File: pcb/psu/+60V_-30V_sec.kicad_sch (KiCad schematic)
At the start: 51 parts, among them J3 Conn_01x03_Socket, J4 Conn_01x03_Socket, U5 ADPL54203, U6 ADPL54203

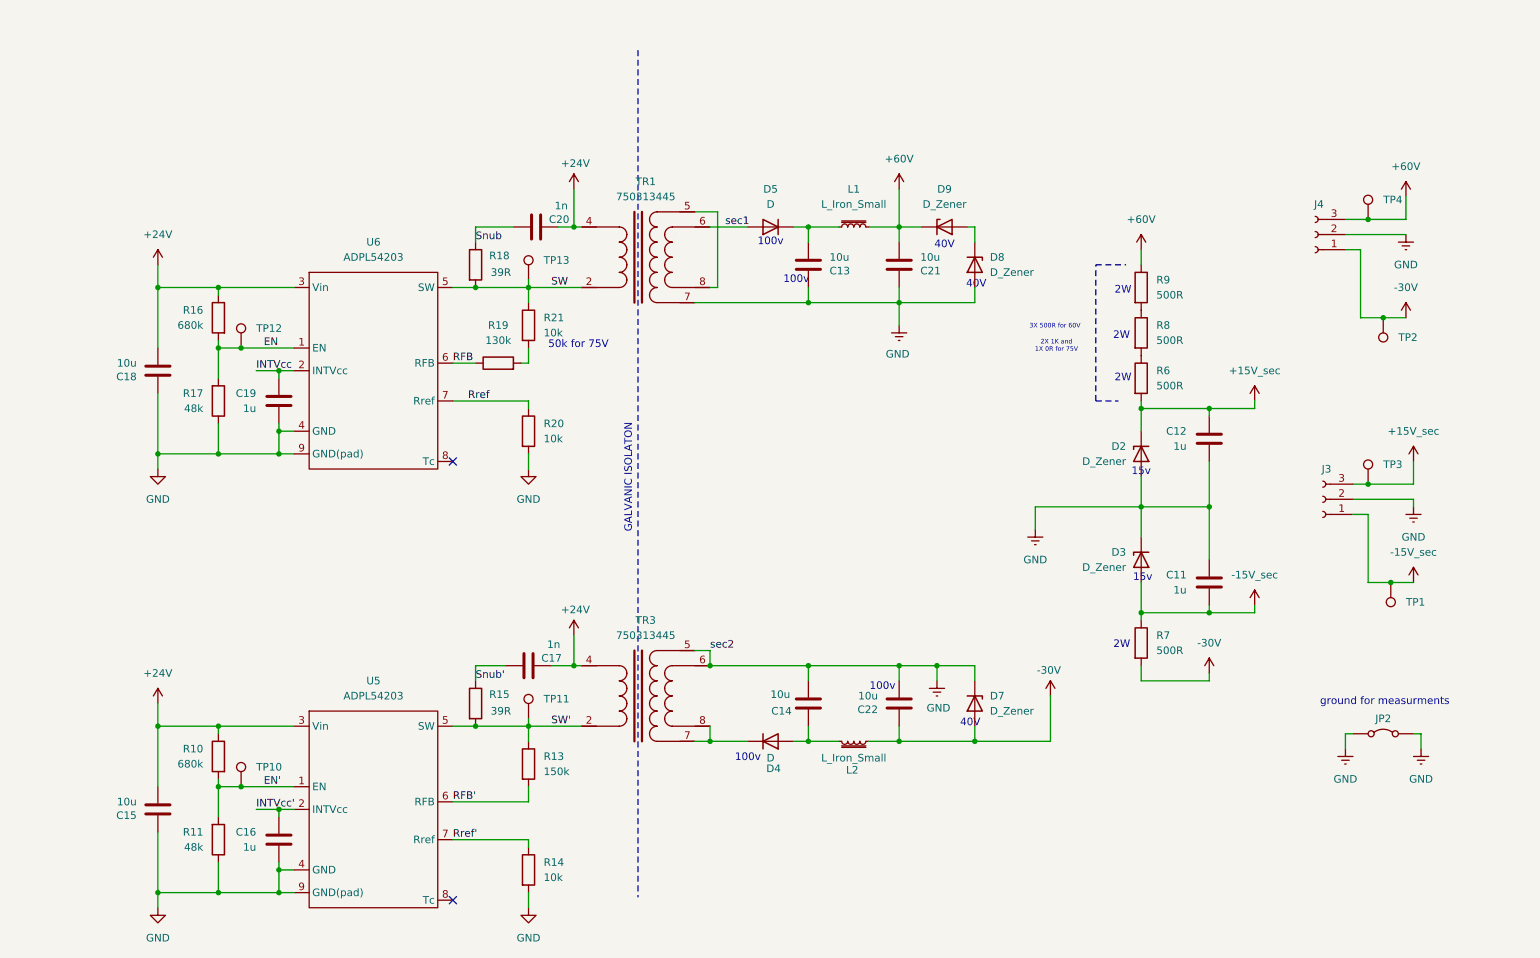
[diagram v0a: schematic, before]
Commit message: poprawki do schematu psu
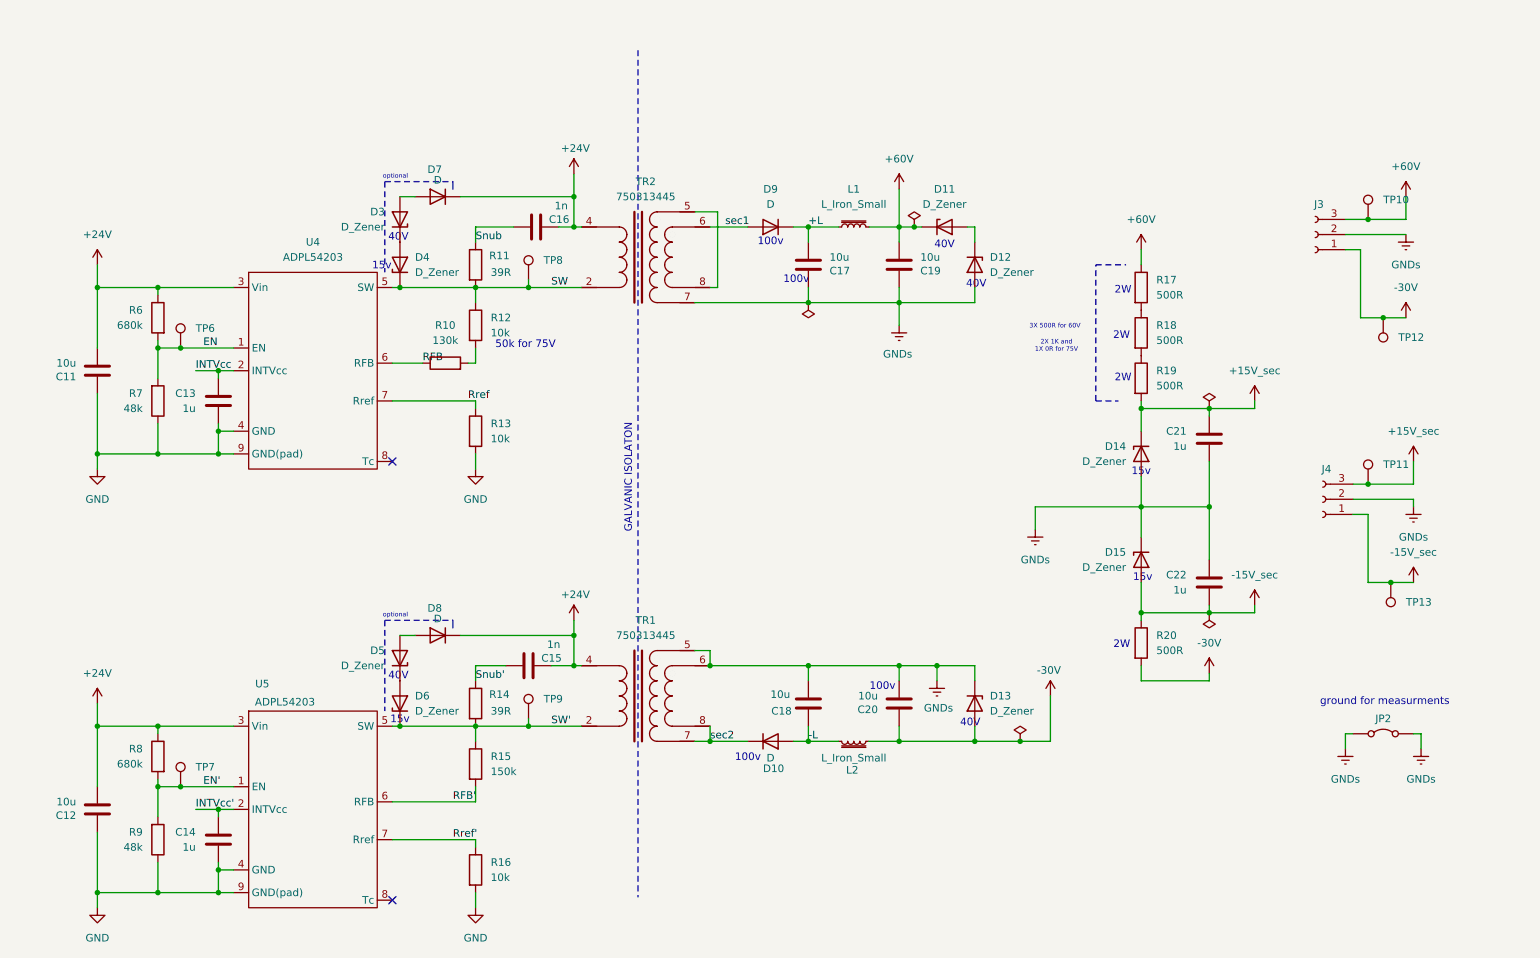
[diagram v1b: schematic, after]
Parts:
- removed TR3: 750313445, Transformer_SMD:Transformer_Wurth_WE-AGDT-EP7, symbol New_Library:750313445
- added D3, D4, D5, D6: D_Zener, symbol Device:D_Zener
- added D7, D8: D, symbol Device:D
- added TR2: 750313445, Library:750313445, symbol New_Library:750313445
- TR1: footprint Transformer_SMD:Transformer_Wurth_WE-AGDT-EP7 -> Library:750313445
- renumbered C18 to C11, C15 to C12, C19 to C13, C16 to C14, C17 to C15, C20 to C16, C13 to C17, C14 to C18, C21 to C19, C22 to C20, C12 to C21, C11 to C22, D4 to D10, D9 to D11, D8 to D12, D7 to D13, D2 to D14, D3 to D15, D5 to D9, J4 to J3, J3 to J4, R19 to R10, R18 to R11, R21 to R12, R20 to R13, R15 to R14, R13 to R15, R14 to R16, R9 to R17, R8 to R18, R6 to R19, R7 to R20, R16 to R6, R17 to R7, R10 to R8, R11 to R9, TP4 to TP10, TP3 to TP11, TP2 to TP12, TP1 to TP13, TP12 to TP6, TP10 to TP7, TP13 to TP8, TP11 to TP9, U6 to U4
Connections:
- net +24V: now also D7.1 (K), D8.1 (K), TR2.4
- net GND: no longer C17.1, C18.2, C19.1, C20.2, C21.2, C22.1, D12.2 (A), D13.1 (K), D14.2 (A), D15.1 (K), J3.2 (Pin_2), J4.2 (Pin_2), JP2.1 (A), JP2.2 (B), TR1.7
- net SW: now also D4.1 (K), TR2.2; no longer TR1.2
- net SW': now also TR1.2, D6.1 (K)
- net sec1: now also TR2.6; no longer TR1.6
- net -L: now reaches C18.1, D10.2 (A), L2.2
- net GNDs: now reaches TR1.5
- net GNDs: now also C17.1, C18.2, C19.1, C20.2, C21.2, C22.1, D12.2 (A), D13.1 (K), D14.2 (A), D15.1 (K), J3.2 (Pin_2), J4.2 (Pin_2), JP2.1 (A), JP2.2 (B), TR1.6, TR2.7; no longer TR1.8
- net +L: now reaches C17.2, D9.1 (K), L1.1
- net sec2: now reaches D10.1 (K)
- net sec2: now also TR1.7, TR1.8
- new net: D5.1 (K), D6.2 (A)
- new net: D5.2 (A), D8.2 (A)
- new net: D3.1 (K), D4.2 (A)
- new net: TR2.5, TR2.8
- new net: D3.2 (A), D7.2 (A)
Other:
- note added: "optional"
- moved on the sheet: C11, C12, C13, C14, R10, R12, R13, R15, R16, R6, R7, R8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

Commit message: added PSU PCB design files
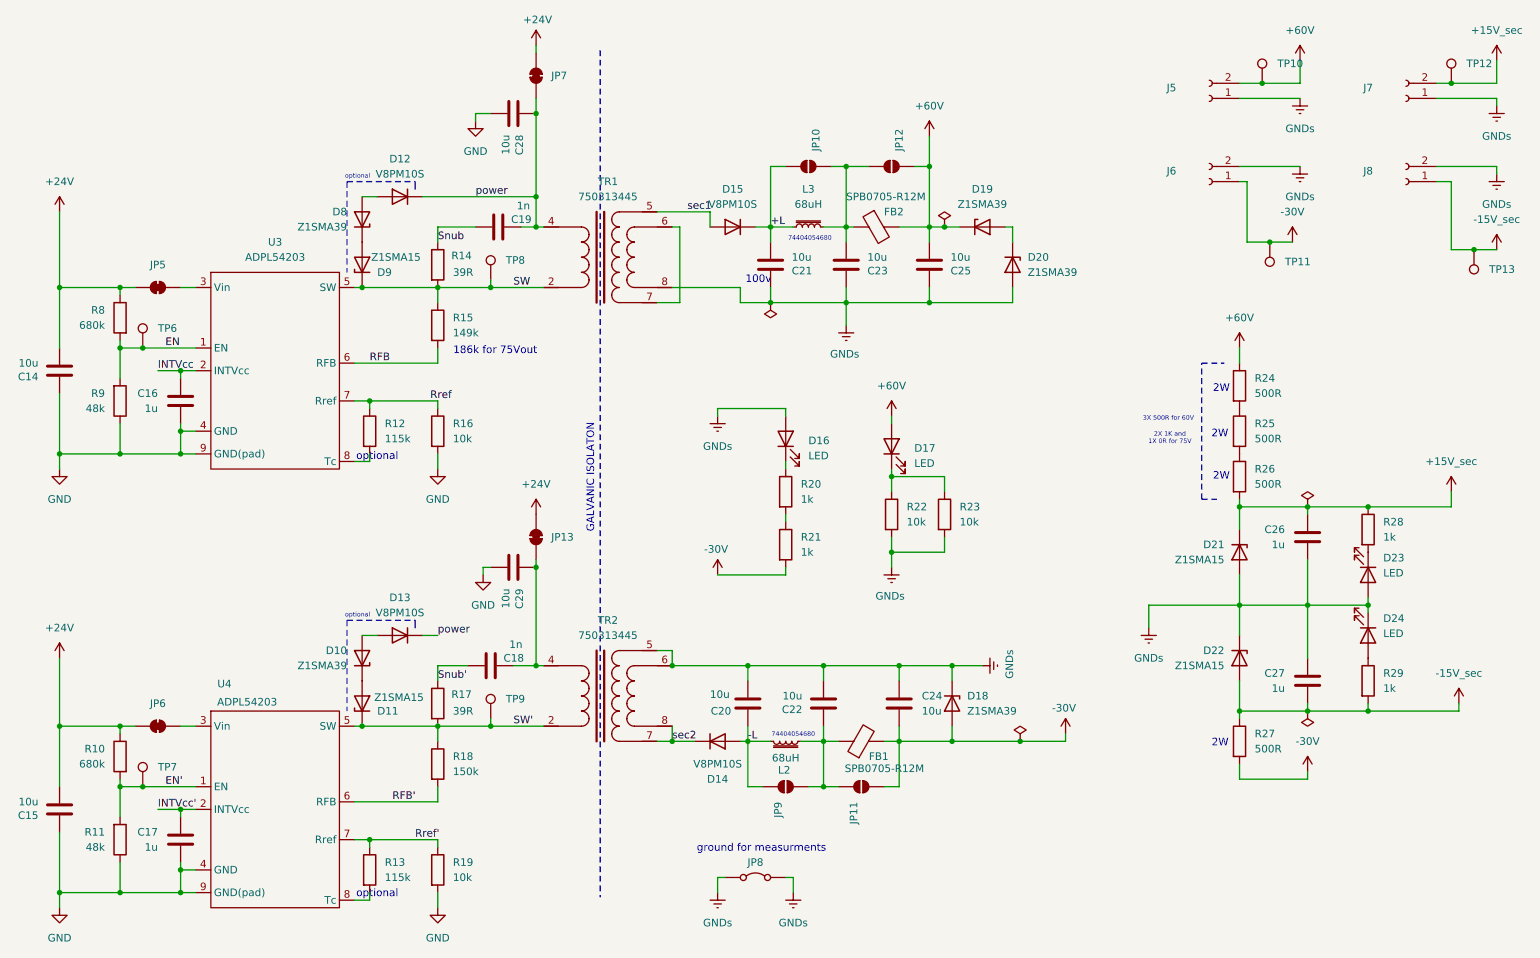
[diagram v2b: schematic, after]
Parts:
- removed D10, D7, D8, D9: D, symbol Device:D
- removed D11, D12, D13, D14, D15, D3, D4, D5, D6: D_Zener, symbol Device:D_Zener
- removed J3, J4: Conn_01x03_Socket, symbol Connector:Conn_01x03_Socket
- removed R10: 130k, symbol Device:R
- added C24, C28, C29: 10u, Capacitor_SMD:C_0805_2012Metric, symbol Device:C
- added C25: 10u, Capacitor_SMD:C_1210_3225Metric, symbol Device:C
- added D10, D18, D19, D20, D8: Z1SMA39, Diode_SMD:D_SMA, symbol Diode:Z1SMAxxx
- added D11, D21, D22, D9: Z1SMA15, Diode_SMD:D_SMA, symbol Diode:Z1SMAxxx
- added D12, D13, D14, D15: V8PM10S, Package_TO_SOT_SMD:TO-277A, symbol Diode:VS-6ESU06
- added D16, D17, D23, D24: LED, LED_SMD:LED_0603_1608Metric, symbol Device:LED
- added FB1, FB2: SPB0705-R12M, Inductor_SMD:L_Coilcraft_1515SQ-68N, symbol Device:FerriteBead
- added J5, J6, J7, J8: Conn_01x02_Socket, Connector_Wago:Wago_734-132_1x02_P3.50mm_Vertical, symbol Connector:Conn_01x02_Socket
- added JP10, JP11, JP12, JP9: SolderJumper_2_Open, Jumper:SolderJumper-2_P1.3mm_Open_RoundedPad1.0x1.5mm, symbol Jumper:SolderJumper_2_Open
- added JP13, JP5, JP6, JP7: SolderJumper_2_Bridged, Jumper:SolderJumper-2_P1.3mm_Bridged2Bar_RoundedPad1.0x1.5mm, symbol Jumper:SolderJumper_2_Bridged
- added R12, R13: 115k, Resistor_SMD:R_0805_2012Metric, symbol Device:R
- added R20, R21, R28, R29: 1k, Resistor_SMD:R_0805_2012Metric, symbol Device:R
- added R22, R23: 10k, Resistor_SMD:R_0805_2012Metric, symbol Device:R
- C14: renamed from C11; footprint (none) -> Capacitor_SMD:C_0805_2012Metric
- C15: renamed from C12; footprint (none) -> Capacitor_SMD:C_0805_2012Metric
- C16: renamed from C13; footprint (none) -> Capacitor_SMD:C_0805_2012Metric
- C17: renamed from C14; footprint (none) -> Capacitor_SMD:C_0805_2012Metric
- C18: renamed from C15; footprint (none) -> Capacitor_SMD:C_0805_2012Metric
- C19: renamed from C16; footprint (none) -> Capacitor_SMD:C_0805_2012Metric
- C20: renamed from C18; footprint (none) -> Capacitor_SMD:C_0805_2012Metric
- C21: renamed from C17; footprint (none) -> Capacitor_SMD:C_1210_3225Metric
- C22: renamed from C20; footprint (none) -> Capacitor_SMD:C_0805_2012Metric
- C23: renamed from C19; footprint (none) -> Capacitor_SMD:C_1210_3225Metric
- C26: renamed from C21; footprint (none) -> Capacitor_SMD:C_0805_2012Metric
- C27: renamed from C22; footprint (none) -> Capacitor_SMD:C_0805_2012Metric
- JP8: renamed from JP2; footprint (none) -> Capacitor_THT:C_Axial_L12.0mm_D6.5mm_P15.00mm_Horizontal
- L2: value L_Iron_Small -> 68uH; footprint (none) -> Inductor_SMD:L_Wuerth_MAPI-5030
- L3: renamed from L1; value L_Iron_Small -> 68uH; footprint (none) -> Inductor_SMD:L_Wuerth_MAPI-5030
- R10: renamed from R8; footprint (none) -> Resistor_SMD:R_0805_2012Metric
- R11: renamed from R9; footprint (none) -> Resistor_SMD:R_0805_2012Metric
- R14: renamed from R11; footprint (none) -> Resistor_SMD:R_2512_6332Metric
- R15: renamed from R12; value 10k -> 149k; footprint (none) -> Resistor_SMD:R_0805_2012Metric
- R16: renamed from R13; footprint (none) -> Resistor_SMD:R_0805_2012Metric
- R17: renamed from R14; footprint (none) -> Resistor_SMD:R_2512_6332Metric
- R18: renamed from R15; footprint (none) -> Resistor_SMD:R_0805_2012Metric
- R19: renamed from R16; footprint (none) -> Resistor_SMD:R_0805_2012Metric
- R24: renamed from R17; footprint (none) -> Resistor_SMD:R_2512_6332Metric
- R25: renamed from R18; footprint (none) -> Resistor_SMD:R_2512_6332Metric
- R26: renamed from R19; footprint (none) -> Resistor_SMD:R_2512_6332Metric
- R27: renamed from R20; footprint (none) -> Resistor_SMD:R_2512_6332Metric
- R8: renamed from R6; footprint (none) -> Resistor_SMD:R_0805_2012Metric
- R9: renamed from R7; footprint (none) -> Resistor_SMD:R_0805_2012Metric
- TP10, TP13, TP6, TP7, TP8, TP9: footprint (none) -> TestPoint:TestPoint_Pad_D1.5mm
- TP11: renamed from TP12; footprint (none) -> TestPoint:TestPoint_Pad_D1.5mm
- TP12: renamed from TP11; footprint (none) -> TestPoint:TestPoint_Pad_D1.5mm
- renumbered TR2 to TR1, TR1 to TR2, U4 to U3, U5 to U4
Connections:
- net +15V_sec: now also D21.1 (K), J7.2 (Pin_2), R28.1
- net +24V: now also JP13.1 (A), JP5.2 (B), JP6.2 (B), JP7.2 (B); no longer C18.2, C19.2, TR1.4, TR2.4, U3.3 (Vin), U4.3 (Vin)
- net +60V: now also C25.2, D17.2 (A), D19.1 (K), FB2.2, J5.2 (Pin_2), JP12.1 (A); no longer C23.2, L3.2
- net +L: now also D15.3 (K), JP10.2 (B)
- net -15V_sec: now also D22.2 (A), J8.1 (Pin_1), R29.2
- net -30V: now also C24.2, D18.2 (A), FB1.2, J6.1 (Pin_1), JP11.2 (B), R21.2; no longer C22.1, L2.1
- net -L: now also D14.1 (A), D14.2 (A), JP9.1 (A)
- net GND: now also C28.2, C29.2
- net GNDs: now also TR1.8, C24.1, C25.1, D16.2 (A), D18.1 (K), D20.2 (A), D21.2 (A), D22.1 (K), D23.2 (A), D24.1 (K), J5.1 (Pin_1), J6.2 (Pin_2), J7.1 (Pin_1), J8.2 (Pin_2), R22.2, R23.2; no longer TR1.7
- net RFB: now also R15.2
- net Rref: now also R12.1
- net Rref': now also R13.1
- net SW: now also D9.1 (K)
- net SW': now also D11.1 (K)
- net sec1: now also TR1.5, D15.1 (A), D15.2 (A); no longer TR1.6
- net sec2: now also D14.3 (K)
- net at U4.8 (Tc): now also R13.2
- net at U3.8 (Tc): now also R12.2
- new net: C23.2, FB2.1, JP10.1 (A), JP12.2 (B), L3.2
- new net: D24.2 (A), R29.1
- new net: D16.1 (K), R20.1
- new net: D23.1 (K), R28.2
- new net: JP5.1 (A), U3.3 (Vin)
- new net: C22.1, FB1.1, JP11.1 (A), JP9.2 (B), L2.1
- new net: D17.1 (K), R22.1, R23.1
- new net: D10.1 (K), D11.2 (A)
- new net: D10.2 (A), D13.1 (A), D13.2 (A)
- new net: D8.1 (K), D9.2 (A)
- new net: D12.1 (A), D12.2 (A), D8.2 (A)
- new net: C18.2, C29.1, JP13.2 (B), TR2.4
- new net: D19.2 (A), D20.1 (K)
- new net: R20.2, R21.1
- new net: JP6.1 (A), U4.3 (Vin)
- new net: TR1.6, TR1.7
- new net power: C19.2, C28.1, D12.3 (K), D13.3 (K), JP7.1 (A), TR1.4
- no-connect marks 2 -> 0
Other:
- note added: "186k for 75Vout"
- note added: "74404054680"
- note removed: "15v"
- note removed: "40V"
- note removed: "50k for 75V"
- moved on the sheet: C14, C15, C16, C17, C18, C19, C20, C21, C22, C23, C26, C27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
